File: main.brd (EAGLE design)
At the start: 160 x 100 mm, 45 parts, among them IC10 FGPMMOPA6H, IC2 25LC1024-I/P, IC6 MPL3115A2LGA, IC7 FXAS21000, IC8 ADXL343BCCZ, Q1 12MHz, U1 ATMEGA1284P-PU, U2 LTC3440EMSPBF

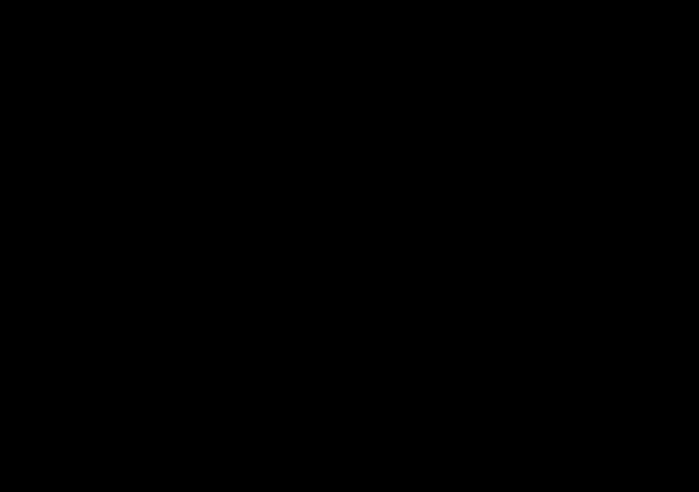
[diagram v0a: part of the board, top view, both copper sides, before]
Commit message: Added datasheet for MCP9700A temperature sensor and added ambient temperature sensor to schematic.
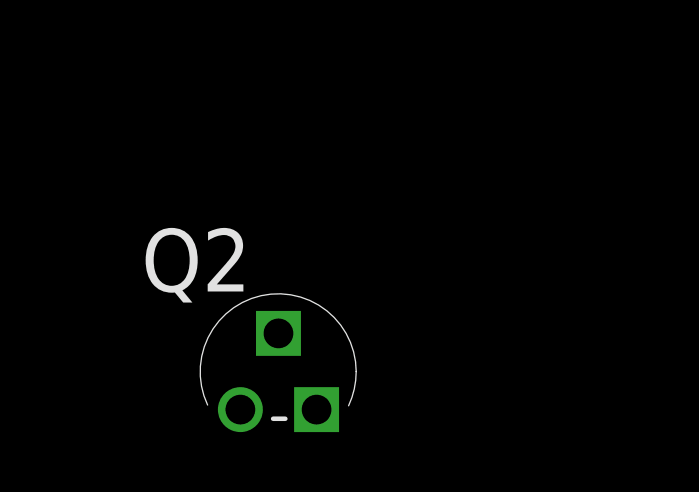
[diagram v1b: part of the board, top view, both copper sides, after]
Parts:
- added Q2: MCP9700A-E/TO, CU in Space:TO127P254X533-3
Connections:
- removed net U2_TRIGGER: U1.1
- new net TEMP: Q2.2, U1.40
- net GND: now also Q2.3
- net VCC: now also Q2.1
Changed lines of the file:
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@@
 <element name="C10" library="rcl" library_urn="urn:adsk.eagle:library:334" package="C025-025X050" package3d_urn="urn:adsk.eagle:package:23629/2" value="47pF" x="-193.04" y="-251.46"/>
 <element name="C11" library="rcl" library_urn="urn:adsk.eagle:library:334" package="C025-025X050" package3d_urn="urn:adsk.eagle:package:23629/2" value="1µF" x="-176.53" y="-251.46"/>
+<element name="Q2" library="CU in Space" package="TO127P254X533-3" value="MCP9700A-E/TO" x="-190.5" y="-266.7">
+<attribute name="MPN" value="MCP9700A-E/TO" x="-190.5" y="-266.7" size="1.778" layer="27" display="off"/>
+<attribute name="OC_FARNELL" value="1332164" x="-190.5" y="-266.7" size="1.778" layer="27" display="off"/>
+<attribute name="OC_NEWARK" value="17M0676" x="-190.5" y="-266.7" size="1.778" layer="27" display="off"/>
+<attribute name="PACKAGE" value="TO-92-3" x="-190.5" y="-266.7" size="1.778" layer="27" display="off"/>
+<attribute name="SUPPLIER" value="Microchip" x="-190.5" y="-266.7" size="1.778" layer="27" display="off"/>
+</element>
 </elements>
 <signals>
@@
 <contactref element="C10" pad="2"/>
 <contactref element="C11" pad="2"/>
+<contactref element="Q2" pad="3"/>
 <wire x1="-175.514" y1="-78.74" x2="-160.274" y2="-78.74" width="0" layer="19" extent="1-1"/>
 <wire x1="-175.26" y1="-64.77" x2="-175.514" y2="-78.74" width="0" layer="19" extent="1-1"/>
@@
 <wire x1="-191.77" y1="-251.46" x2="-193.88" y2="-233.79" width="0" layer="19" extent="1-1"/>
 <wire x1="-175.26" y1="-251.46" x2="-191.77" y2="-251.46" width="0" layer="19" extent="1-1"/>
+<wire x1="-190.5" y1="-269.24" x2="-191.77" y2="-251.46" width="0" layer="19" extent="1-1"/>
 <wire x1="-127" y1="-22.86" x2="-175.26" y2="-50.8" width="0" layer="19" extent="1-1"/>
 <wire x1="-124.46" y1="-22.86" x2="-127" y2="-22.86" width="0" layer="19" extent="1-1"/>
@@
 <contactref element="C10" pad="1"/>
 <contactref element="C11" pad="1"/>
+<contactref element="Q2" pad="1"/>
 <wire x1="-193.3956" y1="-92.4306" x2="-162.306" y2="-78.74" width="0" layer="19" extent="1-1"/>
 <wire x1="-189.23" y1="-50.8" x2="-162.306" y2="-78.74" width="0" layer="19" extent="1-1"/>
@@
 <wire x1="-194.31" y1="-251.46" x2="-193.88" y2="-215.79" width="0" layer="19" extent="1-1"/>
 <wire x1="-177.8" y1="-251.46" x2="-194.31" y2="-251.46" width="0" layer="19" extent="1-1"/>
+<wire x1="-193.04" y1="-269.24" x2="-194.31" y2="-251.46" width="0" layer="19" extent="1-1"/>
 <wire x1="-132.08" y1="-15.24" x2="-189.23" y2="-50.8" width="0" layer="19" extent="1-1"/>
 <wire x1="-152.4" y1="53.34" x2="-132.08" y2="-15.24" width="0" layer="19" extent="1-1"/>
@@
 <contactref element="IC10" pad="P$5"/>
 </signal>
-<signal name="U2_TRIGGER">
-<contactref element="U1" pad="1"/>
-</signal>
 <signal name="U2_RESET">
 <contactref element="ICSP" pad="7"/>
@@
 <wire x1="-181.73" y1="-150.26" x2="-152.145" y2="-200.66" width="0" layer="19" extent="1-1"/>
 </signal>
+<signal name="TEMP">
+<contactref element="Q2" pad="2"/>
+<contactref element="U1" pad="40"/>
+<wire x1="-29.21" y1="54.61" x2="-191.77" y2="-266.7" width="0" layer="19" extent="1-1"/>
+</signal>
 </signals>

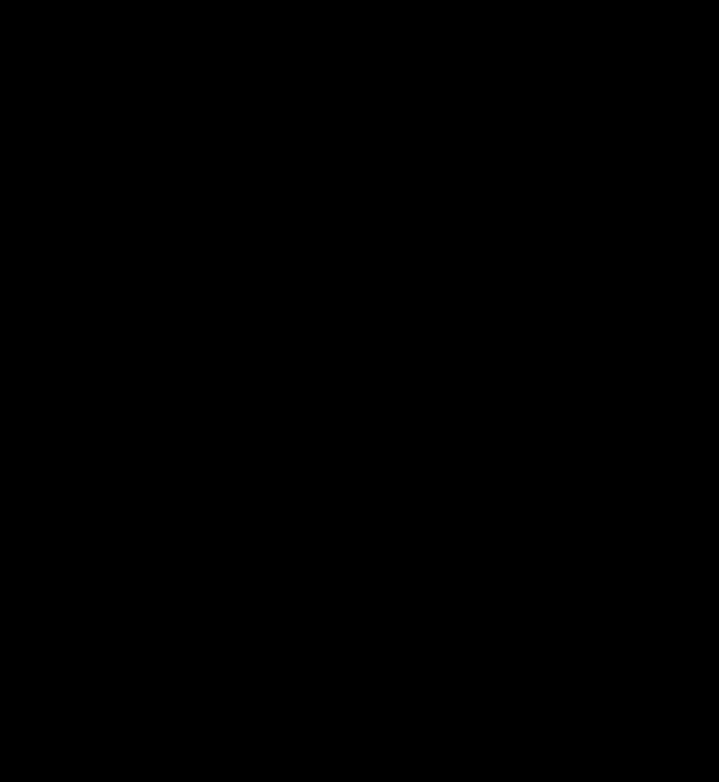
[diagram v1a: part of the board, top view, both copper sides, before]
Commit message: Added high value pullups to SPI CS pins to avoid problems during programming
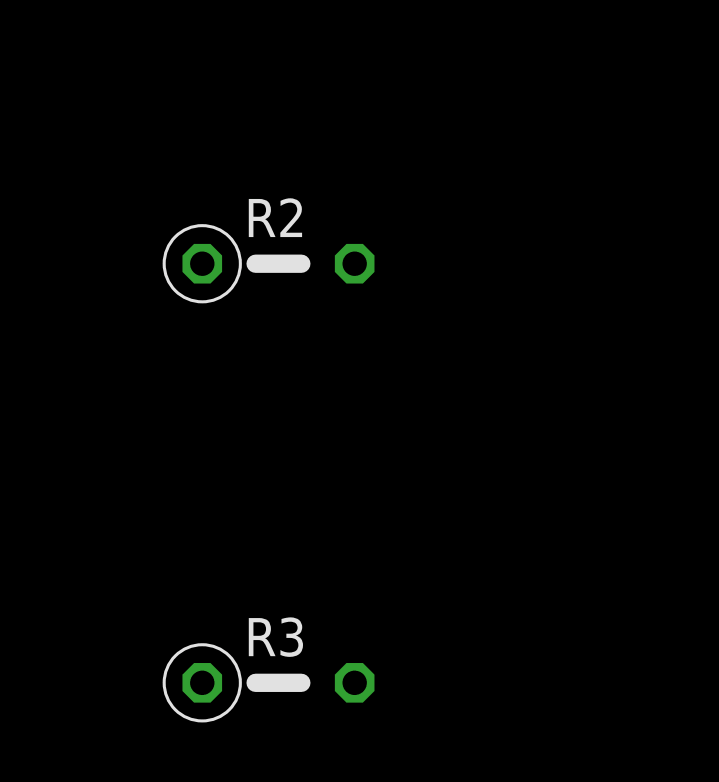
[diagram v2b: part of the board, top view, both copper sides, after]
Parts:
- added R2, R3: 1MΩ, rcl:0207/5V
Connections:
- net EEPROM_CS: now also R2.1
- net RADIO_CS: now also R3.1
- net VCC: now also R2.2, R3.2
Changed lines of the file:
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@@
 <attribute name="SUPPLIER" value="Microchip" x="-190.5" y="-266.7" size="1.778" layer="27" display="off"/>
 </element>
+<element name="R2" library="rcl" library_urn="urn:adsk.eagle:library:334" package="0207/5V" package3d_urn="urn:adsk.eagle:package:23502/1" value="1MΩ" x="-191.77" y="-284.48"/>
+<element name="R3" library="rcl" library_urn="urn:adsk.eagle:library:334" package="0207/5V" package3d_urn="urn:adsk.eagle:package:23502/1" value="1MΩ" x="-191.77" y="-298.45"/>
 </elements>
 <signals>
@@
 <contactref element="C11" pad="1"/>
 <contactref element="Q2" pad="1"/>
+<contactref element="R2" pad="2"/>
+<contactref element="R3" pad="2"/>
 <wire x1="-193.3956" y1="-92.4306" x2="-162.306" y2="-78.74" width="0" layer="19" extent="1-1"/>
 <wire x1="-189.23" y1="-50.8" x2="-162.306" y2="-78.74" width="0" layer="19" extent="1-1"/>
@@
 <wire x1="-177.8" y1="-251.46" x2="-194.31" y2="-251.46" width="0" layer="19" extent="1-1"/>
 <wire x1="-193.04" y1="-269.24" x2="-194.31" y2="-251.46" width="0" layer="19" extent="1-1"/>
+<wire x1="-189.23" y1="-284.48" x2="-193.04" y2="-269.24" width="0" layer="19" extent="1-1"/>
+<wire x1="-189.23" y1="-298.45" x2="-189.23" y2="-284.48" width="0" layer="19" extent="1-1"/>
 <wire x1="-132.08" y1="-15.24" x2="-189.23" y2="-50.8" width="0" layer="19" extent="1-1"/>
 <wire x1="-152.4" y1="53.34" x2="-132.08" y2="-15.24" width="0" layer="19" extent="1-1"/>
@@
 <contactref element="U1" pad="5"/>
 <contactref element="XB2" pad="17"/>
+<contactref element="R3" pad="1"/>
+<wire x1="-171.88" y1="-221.79" x2="-194.31" y2="-298.45" width="0" layer="19" extent="1-1"/>
 <wire x1="-44.45" y1="44.45" x2="-171.88" y2="-221.79" width="0" layer="19" extent="1-1"/>
 </signal>
@@
 <contactref element="U1" pad="4"/>
 <contactref element="IC2" pad="1"/>
+<contactref element="R2" pad="1"/>
+<wire x1="-132.08" y1="-22.86" x2="-194.31" y2="-284.48" width="0" layer="19" extent="1-1"/>
 <wire x1="-44.45" y1="46.99" x2="-132.08" y2="-22.86" width="0" layer="19" extent="1-1"/>
 </signal>

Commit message: Voltage Regulator added
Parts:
- removed BAT1: (no value), adafruit:JST-PH-2-THM
- removed C24: 22µF, rcl:E2-5
- removed C25: 1.5nF, rcl:C025-025X050
- removed RT1: 60.4kΩ, rcl:0207/5V
- added C12, C15: 1n, Power:2.5MM_CAP
- added C13, C14: 22u, Power:2.5MM_AL_CAP
- added C16: 10n, Power:2.5MM_CAP
- added C18, C20: (no value), Power:2.5MM_CAP
- added C19: (no value), Power:2.5MM_AL_CAP
- added D1, D2, D3: (no value), Power:11.6MM_D
- added L1: 18u, Power:5.4MM_L
- added R11: 24.9k, Power:YAG_MF25
- added R12: 51.1k, Power:YAG_MF25
- added R13: 17.4k, Power:YAG_MF25
- added R14, R15: (no value), Power:YAG_MF25
- added R7: 8.06k, Power:YAG_MF25
- added U3: 2N3904BU, Power:TO-92
- C7: value 10µF -> 10n; device rcl:E2-5 -> Power:2.5MM_CAP
- L3: value 10µH -> (none); device rcl:0207/5V -> Power:14MM_L
- R10: value 15kΩ -> 24.9k; device rcl:0207/5V -> Power:YAG_MF25
- R8: value 340kΩ -> 51.1k; device rcl:0207/5V -> Power:YAG_MF25
- R9: value 200kΩ -> 3.65k; device rcl:0207/5V -> Power:YAG_MF25
- U2: value LTC3440EMSPBF -> LT3570EFEPBF; device CU in Space:SOP50P490X110-10N -> Power:TSSOP-20_FE/CB
- moved L3 440.8 mm to (-208.3, -476.2)
- moved R10 359.6 mm to (-204.5, -424.2)
- moved R9 359.5 mm to (-204.5, -408.9)
- moved R8 343.1 mm to (-204.5, -393.7)
- moved C7 249.2 mm to (-204.5, -326.4)
- moved U2 207.3 mm to (-205.7, -298.4)
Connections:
- removed net FB: R10.1, R8.1, R9.2, U2.9
- removed net N$14: C25.1, U2.10
- removed net VBAT1: BAT1.1, C7.+, U2.7, U2.8
- new net +12.0: C14.1, D1.1, R8.1
- new net +2.5: C20.1, R14.1, U3.1
- new net FB1: R8.2, R9.1, U2.1
- new net N$15: R12.1, R13.2, U2.9
- new net N$16: C18.1, D3.1, U2.13
- new net N$17: R14.2, R15.1, U2.10
- new net N$5: C7.1, U2.7
- new net N$6: R7.2, U2.6
- new net N$7: R10.2, U2.8
- new net N$8: D1.2, L1.2, U2.16
- new net N$9: C15.1, R11.2
- new net NPN_DRV: U2.11, U3.2
- new net PWR_JUNC: C13.1, L1.1, U2.12, U2.14, U2.18, U2.2, U2.3, U2.4
- net GND: now also C12.2, C13.2, C14.2, C15.2, C16.2, C19.2, C20.2, C7.2, D2.2, R13.1, R15.2, R7.1, R9.2, U2.17, U2.5; no longer BAT1.2, C24.-, C7.-, R9.1, RT1.1, U2.2
- net N$10: now also C12.1, R10.1; no longer L3.1, U2.3
- net N$11: now also R11.1, U2.20; no longer L3.2, U2.4
- net N$12: now also C16.1, U2.19; no longer RT1.2, U2.1
- net N$13: now also C18.2, D2.1, L3.1, U2.15; no longer C25.2, R10.2
- net VCC: now also C19.1, D3.2, L3.2, R12.2, U3.3; no longer C24.+, R8.2, U2.6

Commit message: Power_Fixed
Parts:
- removed C18: (no value), Power:2.5MM_CAP
- added DC1: PJ-102BH, Power:DC_JACK_3
- added Q3: FQP7P06, Power:PMOS
- added R16: 51.1kΩ, Power:YAG_MF25
- added XLR1: NC3FAH1, Power:NC3FAH1
- added XLR2: NC5FAH, Power:NC5FAH
- C1, C27, C28: value 100nF -> 0.1µF
- C12, C15: value 1n -> 1nF
- C13, C14: value 22u -> 22µF
- C16, C7: value 10n -> 10nF
- C19: value (none) -> 22µF
- C20: value (none) -> 0.1µF; device Power:2.5MM_CAP -> rcl:C025-025X050
- L1: value 18u -> 18µH
- L3: value (none) -> 4.7µH
- R10, R11: value 24.9k -> 24.9kΩ
- R12, R8: value 51.1k -> 51.1kΩ
- R13: value 17.4k -> 17.4kΩ
- R14: value (none) -> 3.65kΩ
- R15: value (none) -> 51.1kΩ
- R7: value 8.06k -> 8.06kΩ
- R9: value 3.65k -> 3.65kΩ
- U3: value 2N3904BU -> TL431BQLP; device Power:TO-92 -> Power:LP3
- moved R15 681.3 mm to (10.8, 38.1), turned to 270 degrees
- moved C19 679.1 mm to (51.3, 61.1), turned to 270 degrees
- moved R14 665.9 mm to (7.62, 38.1), turned to 270 degrees
- moved C20 653.5 mm to (10.0, -10.0)
- moved U3 640.5 mm to (8.89, 24.1)
- moved R13 635.6 mm to (42.9, 36.8), turned to 90 degrees
- moved D3 622.1 mm to (45.6, 61.2), turned to 270 degrees
- moved R12 612.3 mm to (46.3, 25.2), turned to 270 degrees
- moved D2 606.9 mm to (41.3, 61.2), turned to 90 degrees
- moved L3 585.0 mm to (50.8, 48.3), turned to 90 degrees
- moved C16 571.4 mm to (31.6, 49.0), turned to 180 degrees
- moved C15 554.9 mm to (22.9, 46.3)
- moved R11 533.6 mm to (22.1, 43.6), turned to 180 degrees
- moved R10 521.5 mm to (39.6, 36.7), turned to 90 degrees
- moved C14 508.5 mm to (30.7, 64.3)
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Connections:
- removed net +2.5: C20.1, R14.1, U3.1
- removed net N$17: R14.2, R15.1, U2.10
- removed net NPN_DRV: U2.11, U3.2
- new net BAT+: Q3.3, R14.1, R15.1, XLR1.2
- new net N$30: DC1.3, XLR1.1, XLR1.3
- new net N$69: Q3.1, R14.2, U3.1
- new net N$70: R15.2, R16.1, U3.2
- net GND: now also DC1.2, R16.2, U2.4, U2.EPAD, U3.3, XLR2.5; no longer C20.2, R15.2
- net N$13: now also C20.2; no longer C18.2
- net N$16: now also C20.1; no longer C18.1
- net PWR_JUNC: now also DC1.1, Q3.2; no longer U2.12, U2.4
- net VCC: no longer U3.3
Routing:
- net PWR_JUNC: track 0.00 -> 102.4 mm, vias 0 -> 1
- net N$30: track 0.00 -> 59.3 mm
- net VCC: track 0.00 -> 50.9 mm
- net BAT+: track 0.00 -> 46.5 mm
- net +12.0: track 0.00 -> 42.1 mm, vias 0 -> 1
- net N$13: track 0.00 -> 28.3 mm, vias 0 -> 1
- net FB1: track 0.00 -> 23.5 mm
- net N$5: track 0.00 -> 19.1 mm, vias 0 -> 1
- net N$8: track 0.00 -> 17.6 mm, vias 0 -> 1
- net N$69: track 0.00 -> 16.6 mm
- net N$70: track 0.00 -> 16.3 mm
- net N$10: track 0.00 -> 15.6 mm
- net N$12: track 0.00 -> 9.35 mm
- net N$16: track 0.00 -> 9.30 mm
- net N$15: track 0.00 -> 8.58 mm
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- added copper zone on layer 1, net GND
- added copper zone on layer 16, net GND
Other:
- board size 160 x 100 mm -> 55 x 220 mm

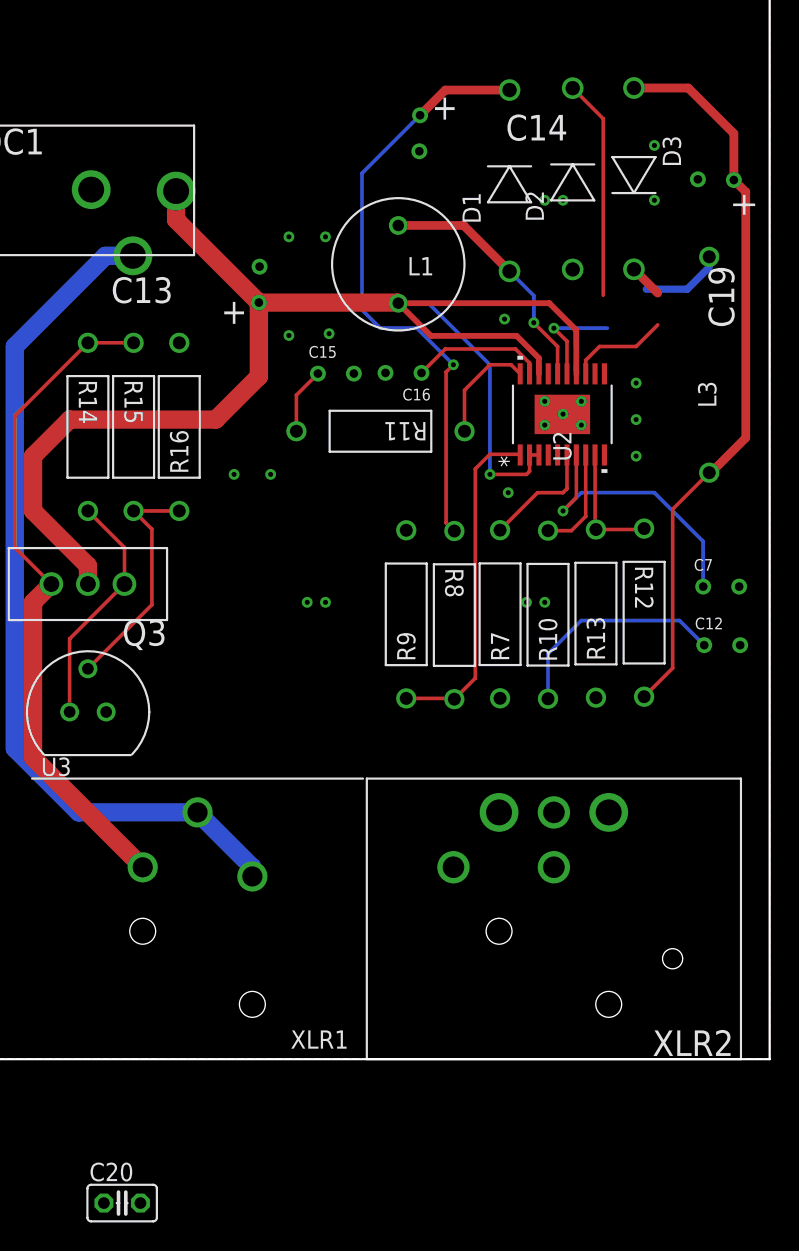
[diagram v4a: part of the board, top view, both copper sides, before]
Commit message: Updated Datasheets
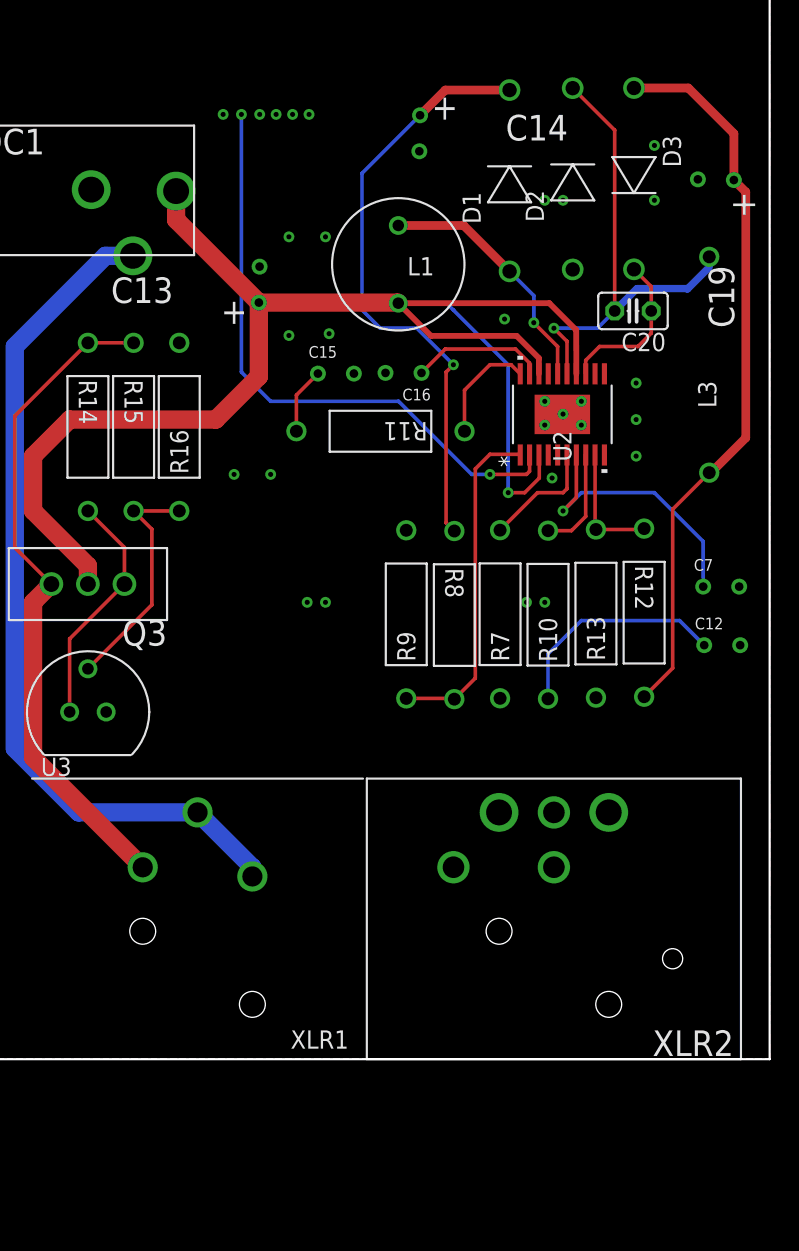
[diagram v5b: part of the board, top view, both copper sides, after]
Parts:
- moved C20 71.4 mm to (45.5, 52.0), turned to 180 degrees
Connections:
- new net 12V_ENABLE: U2.2
- net PWR_JUNC: no longer U2.2
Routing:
- net 12V_ENABLE: track 0.00 -> 42.1 mm, vias 0 -> 2
- net N$13: track 28.3 -> 33.6 mm
- net PWR_JUNC: track 102.4 -> 104.6 mm
- net N$16: track 9.30 -> 11.2 mm

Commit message: Added MCU, Sensors and Radios
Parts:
- removed X2: (no value), adafruit:U.FL
- added C18, C21: 0.1µF, rcl:C025-025X050
- added CONSOLE: (no value), pinhead:1X04
- added Q4: MCP9700A-E/TO, CU in Space:TO127P254X533-3
- added R17, R18: 47kΩ, rcl:0207/5V
- added R19: 2K2Ω, rcl:0207/5V
- added X1: 132134RP, CU in Space:132134RP
- DEBUG: device pinhead:1X04 -> led:LED5MM
- ICSP: device pinhead:2X04 -> pinhead:2X03
- Q1: device crystal:HC33U-V -> special:QS
- moved L2 106.4 mm to (31.8, 194.6), turned to 180 degrees
- moved C17 95.0 mm to (23.5, 119.4), turned to 270 degrees
- moved R6 92.9 mm to (40.6, 195.6), turned to 180 degrees
- moved R5 92.9 mm to (40.6, 199.4), turned to 180 degrees
- moved Q2 91.4 mm to (2.54, 193.0), turned to 180 degrees
- moved C34 88.5 mm to (40.3, 126.5), turned to 180 degrees
- moved IC10 76.7 mm to (45.7, 138.4), turned to 90 degrees
- moved C2 62.1 mm to (5.08, 214.6), turned to 90 degrees
- moved R3 60.9 mm to (17.3, 153.4)
- moved U1 47.4 mm to (52.1, 189.2), turned to 90 degrees
- moved C10 46.2 mm to (10.2, 124.5)
- moved C1 46.0 mm to (15.0, 209.0), turned to 270 degrees
- moved C4 44.4 mm to (27.9, 171.4)
- moved R1 43.4 mm to (12.7, 204.5), turned to 180 degrees
- moved C11 36.8 mm to (10.2, 120.7)
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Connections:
- net U1_RESET renamed RESET
- removed net U2_RESET: ICSP.7
- new net ACCEL_INT: IC8.8, U1.25
- new net ALT_INT: IC6.P$6, U1.24
- new net BAT_REF: C21.1, R17.1, R18.2, U1.33
- new net DEBUG_LED: DEBUG.A, U1.1
- new net GYRO_INT: IC7.3, U1.26
- new net N$71: DEBUG.K, R19.1
- new net TEMP2: Q4.2, U1.39
- net 12V_ENABLE: now also U1.27
- net AVCC: now also C18.2, Q2.1, Q4.1
- net A_GND: now also C18.1, C21.2, Q2.3, Q4.3, R18.1, U1.31
- net BAT+: now also R17.2
- net GND: now also CONSOLE.4, R19.2, X1.1, X1.2, X1.3, X1.4; no longer DEBUG.4, Q2.3, U1.31, X2.1, X2.2
- net N$4: now also X1.0; no longer X2.3
- net RXD0: now also CONSOLE.2; no longer DEBUG.2
- net TXD0: now also CONSOLE.3; no longer DEBUG.3, ICSP.8
- net VCC: now also CONSOLE.1; no longer DEBUG.1, Q2.1
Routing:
- net VCC: track 50.9 -> 449.4 mm, vias 0 -> 2
- net 12V_ENABLE: track 42.1 -> 214.4 mm
- net BAT+: track 46.5 -> 207.2 mm
- net MISO: track 0.00 -> 79.0 mm
- net EEPROM_CS: track 0.00 -> 74.1 mm
- net SDA: track 0.00 -> 66.3 mm
- net SCL: track 0.00 -> 63.2 mm
- net SCK: track 0.00 -> 62.4 mm
- net MOSI: track 0.00 -> 59.8 mm
- net TXD1: track 0.00 -> 55.9 mm
- net RXD1: track 0.00 -> 55.0 mm
- net GYRO_INT: track 0.00 -> 44.5 mm, vias 0 -> 1
- net AVCC: track 0.00 -> 41.2 mm
- net RADIO_CS: track 0.00 -> 24.7 mm
- net RADIO_INT: track 0.00 -> 24.1 mm
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- added copper zone on layer 1, net A_GND
- added copper zone on layer 16, net A_GND
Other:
- board size 55 x 220 mm -> 57.5 x 220 mm
- board text added: "+3.3V"
- board text added: "GND"
- board text added: "GPS Antenna"
- board text added: "MISO"
- board text added: "MOSI"
- board text added: "RESET"
- board text added: "RXD"
- board text added: "SCK"
- board text added: "TXD"
- board text added: "This End Faces Nose"
